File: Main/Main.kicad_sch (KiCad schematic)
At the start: 95 parts, among them J1 USB_B_Micro, J2 XT60, J3 Conn_01x03, J4 Conn_01x03, J5 Conn_01x03, J6 Conn_01x03, J7 MSD-4-A, Q2 Si2301CDS, SW1 SW_Push, SW2 SW_Push, U1 RP2350A-QFN60, U10 LM75B, U11 MCS1802GS-50-Z, U12 MCS1802GS-50-Z, U13 MCS1802GS-50-Z, U15 AP62150WU, U2 W25Q128JVS, U3 AMS1117-3.3, U4 MMC5983MA, U5 ICM-42688-P, U6 INA226, U7 KX134-1211, U8 MS5611-01BA, U9 MCS1802GS-50-Z, Y1 ABM8-272-T3

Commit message: more layout updates and small fixes
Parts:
- D1: value LED -> RED_LED
- D2: value LED -> BLUE_LED
- D3: value LED -> GREEN_LED
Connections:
- net ACCEL_SDI/SDA is gone; now on net SPI_SDI: U7.2 (SDI/SDA)
- net ACCEL_SDO/ADDR is gone; now on net SPI_SD0: U7.1 (SDO/ADDR)
- net GND: now also C29.2, C30.2; no longer R13.1, U6.8 (Vbus), U6.9 (Vin-)
- net VIN: now also R13.1, U6.9 (Vin-); no longer J2.2 (Pin_2)
- net VSS: no longer names the net of R13.2, U6.10 (Vin+)
- net VSS: now also J2.2 (Pin_2), U6.8 (Vbus)
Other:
- moved on the sheet: C24, C39, C40, C41, D1, D2, D3, J2, L3, Q2, R10, R11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

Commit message: more layout updates
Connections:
- net SCL: now also U1.33 (GPIO21)
- net SDA: now also U1.32 (GPIO20)
- net Vout1: now also U1.40 (GPIO26_ADC0)
- net Vout2: now also U1.41 (GPIO27_ADC1)
- net Vout3: now also U1.43 (GPIO29_ADC3)
- net Vout4: now also U1.42 (GPIO28_ADC2)
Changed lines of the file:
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@@
+		)
+	)
+	(global_label "Vout1"
+		(shape input)
+		(at 212.09 143.51 0)
+		(fields_autoplaced yes)
+		(effects
+			(font
+				(size 1.27 1.27)
+			)
+			(justify left)
+		)
+		(property "Intersheetrefs" "${INTERSHEET_REFS}"
+			(at 220.397 143.51 0)
+			(effects
+				(font
+					(size 1.27 1.27)
+				)
+				(justify left)
+				(hide yes)
+			)
 		)
 	)
@@
 		)
 	)
+	(global_label "Vout4"
+		(shape input)
+		(at 212.09 148.59 0)
+		(fields_autoplaced yes)
+		(effects
+			(font
+				(size 1.27 1.27)
+			)
+			(justify left)
+		)
+		(property "Intersheetrefs" "${INTERSHEET_REFS}"
+			(at 220.397 148.59 0)
+			(effects
+				(font
+					(size 1.27 1.27)
+				)
+				(justify left)
+				(hide yes)
+			)
+		)
+	)
 	(global_label "SPI_SDI"
 		(shape input)
@@
 		)
 	)
+	(global_label "SDA"
+		(shape input)
+		(at 212.09 125.73 0)
+		(fields_autoplaced yes)
+		(effects
+			(font
+				(size 1.27 1.27)
+			)
+			(justify left)
+		)
+		(property "Intersheetrefs" "${INTERSHEET_REFS}"
+			(at 218.6433 125.73 0)
+			(effects
+				(font
+					(size 1.27 1.27)
+				)
+				(justify left)
+				(hide yes)
+			)
+		)
+	)
 	(global_label "current -1"
 		(shape input)
@@
 		)
 	)
+	(global_label "Vout3"
+		(shape input)
+		(at 212.09 151.13 0)
+		(fields_autoplaced yes)
+		(effects
+			(font
+				(size 1.27 1.27)
+			)
+			(justify left)
+		)
+		(property "Intersheetrefs" "${INTERSHEET_REFS}"
+			(at 220.397 151.13 0)
+			(effects
+				(font
+					(size 1.27 1.27)
+				)
+				(justify left)
+				(hide yes)
+			)
+		)
+	)
 	(global_label "SPI_SDI2"
 		(shape input)
@@
 				)
 				(justify right)
+				(hide yes)
+			)
+		)
+	)
+	(global_label "Vout2"
+		(shape input)
+		(at 212.09 146.05 0)
+		(fields_autoplaced yes)
+		(effects
+			(font
+				(size 1.27 1.27)
+			)
+			(justify left)
+		)
+		(property "Intersheetrefs" "${INTERSHEET_REFS}"
+			(at 220.397 146.05 0)
+			(effects
+				(font
+					(size 1.27 1.27)
+				)
+				(justify left)
 				(hide yes)
 			)
@@
 			(effects
 				(font
+					(size 1.27 1.27)
+				)
+				(justify left)
+				(hide yes)
+			)
+		)
+	)
+	(global_label "SCL"
+		(shape input)
+		(at 212.09 128.27 0)
+		(fields_autoplaced yes)
+		(effects
+			(font
+				(size 1.27 1.27)
+			)
+			(justify left)
+		)
+		(property "Intersheetrefs" "${INTERSHEET_REFS}"
+			(at 218.5828 128.27 0)
+			(effects
+				(font

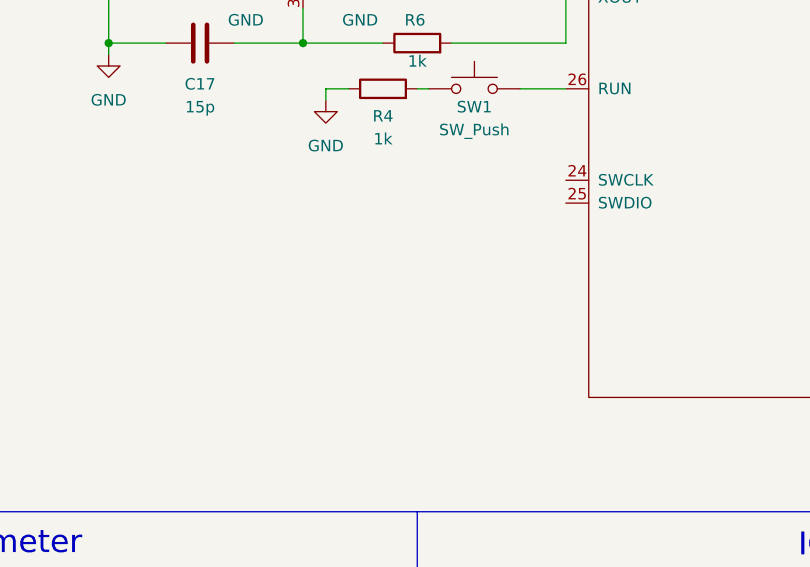
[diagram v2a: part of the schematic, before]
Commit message: updated layout
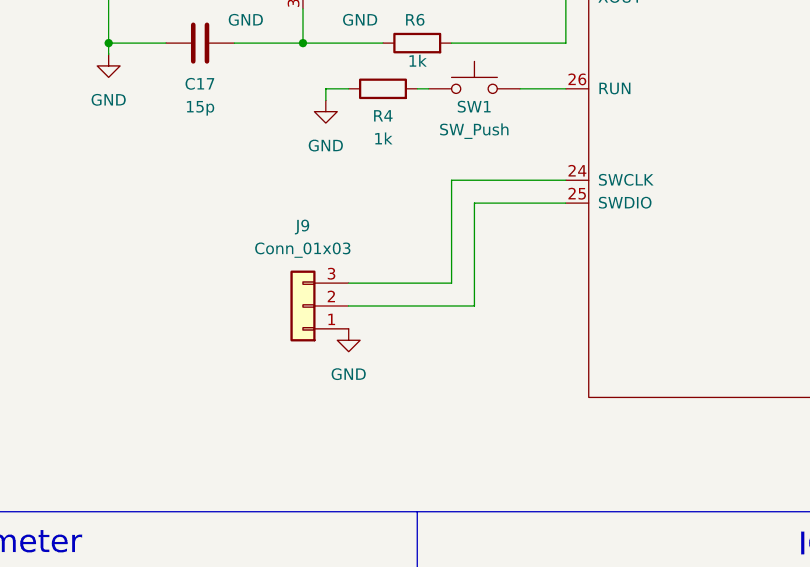
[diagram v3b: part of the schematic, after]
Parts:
- added J9: Conn_01x03, Connector_PinHeader_2.54mm:PinHeader_1x03_P2.54mm_Vertical, symbol Connector_Generic:Conn_01x03
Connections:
- net GND: now also J9.1 (Pin_1)
- net at U1.24 (SWCLK): now also J9.3 (Pin_3)
- net at U1.25 (SWDIO): now also J9.2 (Pin_2)
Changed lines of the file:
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@@
 	(wire
 		(pts
+			(xy 149.86 133.35) (xy 139.7 133.35)
+		)
+		(stroke
+			(width 0)
+			(type default)
+		)
+	)
+	(wire
+		(pts
 			(xy 137.16 60.96) (xy 137.16 62.23)
 		)
@@
 	(wire
 		(pts
+			(xy 125.73 144.78) (xy 139.7 144.78)
+		)
+		(stroke
+			(width 0)
+			(type default)
+		)
+	)
+	(wire
+		(pts
 			(xy 114.3 107.95) (xy 115.57 107.95)
 		)
@@
 	(wire
 		(pts
+			(xy 137.16 130.81) (xy 137.16 142.24)
+		)
+		(stroke
+			(width 0)
+			(type default)
+		)
+	)
+	(wire
+		(pts
 			(xy 345.44 194.31) (xy 347.98 194.31)
 		)
@@
 		)
 	)
+	(wire
+		(pts
+			(xy 137.16 142.24) (xy 125.73 142.24)
+		)
+		(stroke
+			(width 0)
+			(type default)
+		)
+	)
 	(polyline
 		(pts
@@
 	(wire
 		(pts
+			(xy 139.7 133.35) (xy 139.7 144.78)
+		)
+		(stroke
+			(width 0)
+			(type default)
+		)
+	)
+	(wire
+		(pts
 			(xy 22.86 193.04) (xy 34.29 193.04)
 		)
@@
 	(wire
 		(pts
+			(xy 149.86 130.81) (xy 137.16 130.81)
+		)
+		(stroke
+			(width 0)
+			(type default)
+		)
+	)
+	(wire
+		(pts
 			(xy 24.13 44.45) (xy 26.67 44.45)
 		)
@@
 	)
 	(symbol
+		(lib_id "Connector_Generic:Conn_01x03")
+		(at 120.65 144.78 180)
+		(unit 1)
+		(exclude_from_sim no)
+		(in_bom yes)
+		(on_board yes)
+		(dnp no)
+		(fields_autoplaced yes)
+		(property "Reference" "J9"
+			(at 120.65 135.89 0)
+			(effects
+				(font
+					(size 1.27 1.27)
+				)
+			)
+		)
+		(property "Value" "Conn_01x03"
+			(at 120.65 138.43 0)
+			(effects
+				(font
+					(size 1.27 1.27)
+				)
+			)
+		)
+		(property "Footprint" "Connector_PinHeader_2.54mm:PinHeader_1x03_P2.54mm_Vertical"
+			(at 120.65 144.78 0)
+			(effects
+				(font
+					(size 1.27 1.27)
+				)
+				(hide yes)
+			)
+		)
+		(property "Datasheet" "~"
+			(at 120.65 144.78 0)
+			(effects
+				(font
+					(size 1.27 1.27)
+				)
+				(hide yes)
+			)
+		)
+		(property "Description" "Generic connector, single row, 01x03, script generated (kicad-library-utils/schlib/autogen/connector/)"
+			(at 120.65 144.78 0)
+			(effects
+				(font
+					(size 1.27 1.27)
+				)
+				(hide yes)
+			)
+		)
+		(property "JLCPCB Part #" ""
+			(at 120.65 144.78 0)
+			(effects
+				(font
+					(size 1.27 1.27)
+				)
+				(hide yes)
+			)
+		)
+		(property "Sim.Device" ""
+			(at 120.65 144.78 0)
+			(effects
+				(font
+					(size 1.27 1.27)
+				)
+				(hide yes)
+			)
+		)
+		(pin "1"
+		)
+		(pin "2"
+		)
+		(pin "3"
+		)
+		(instances
+			(project "Main"
+				(path "/6b66026e-3aa1-4d5a-a331-be21386153c7"
+					(reference "J9")
+					(unit 1)
+				)
+			)
+		)
+	)
+	(symbol
 		(lib_id "power:GND")
 		(at 502.92 86.36 0)
@@
 					(unit 1)
 				)
+			)
+		)
+	)
+	(symbol
+		(lib_id "power:GND")
+		(at 125.73 147.32 0)
+		(unit 1)
+		(exclude_from_sim no)
+		(in_bom yes)
+		(on_board yes)
+		(dnp no)
+		(fields_autoplaced yes)
+		(property "Reference" "#PWR030"
+			(at 125.73 153.67 0)
+			(effects
+				(font
+					(size 1.27 1.27)
+				)
+				(hide yes)
+			)
+		)
+		(property "Value" "GND"
+			(at 125.73 152.4 0)
+			(effects
+				(font
+					(size 1.27 1.27)
+				)
+			)
+		)
+		(property "Footprint" ""
+			(at 125.73 147.32 0)
+			(effects
+				(font
+					(size 1.27 1.27)
+				)
+				(hide yes)
+			)
+		)
+		(property "Datasheet" ""
+			(at 125.73 147.32 0)
+			(effects
+				(font
+					(size 1.27 1.27)
+				)
+				(hide yes)
+			)
+		)
+		(property "Description" "Power symbol creates a global label with name \"GND\" , ground"
+			(at 125.73 147.32 0)
+			(effects
+				(font
+					(size 1.27 1.27)
+				)
+				(hide yes)
+			)
+		)
+		(pin "1"
+		)
+		(instances
+			(project "Main"
+				(path "/6b66026e-3aa1-4d5a-a331-be21386153c7"
+					(reference "#PWR030")
+					(unit 1)
+				)

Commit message: updated power switching schematic
still need to fix footprint tsp
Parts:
- removed Q2: Si2301CDS, Package_TO_SOT_SMD:SOT-23, symbol Transistor_FET:Si2319CDS
- removed R22: 100k, Resistor_SMD:R_0402_1005Metric, symbol Device:R
- added C35: 1u, Capacitor_SMD:C_0805_2012Metric, symbol Device:C_Small
- added R19, R27: 30k, Resistor_SMD:R_0603_1608Metric, symbol Device:R_Small_US
- added R24, R25, R26: 100k, Resistor_SMD:R_0603_1608Metric, symbol Device:R_Small_US
- added U14: TPS2121RUXR, TPS2121:IC_TPS2121RUXR, symbol TPS2121RUXR:TPS2121RUXR
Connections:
- net +3.3V: no longer C21.1, U3.2 (VO)
- net GND: now also C35.2, R24.2, R26.2, R27.2, U14.12 (GND), U14.4 (OV2), U14.5 (OV1), U14.9 (ST)
- net 3.3v_Batt: now reaches C41.1, L3.1, R20.1
- net 3.3v_Batt: now also R25.1, U14.2 (IN2), U14.2_1 (IN2)
- new net: R25.2, R26.1, U14.3 (CP2)
- new net: R19.2, R24.1, U14.6 (PR1)
- new net: R27.1, U14.10 (ILIM)
- new net: C35.1, U14.11 (SS)
- new net 3.3v_usb: C21.1, R19.1, U14.7 (IN1), U14.7_1 (IN1), U3.2 (VO)
- new net OUT: U14.1 (OUT), U14.1_1 (OUT), U14.8 (OUT), U14.8_1 (OUT)
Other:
- note removed: "Blocks Connection when USB plugged in to prevent backpowering"

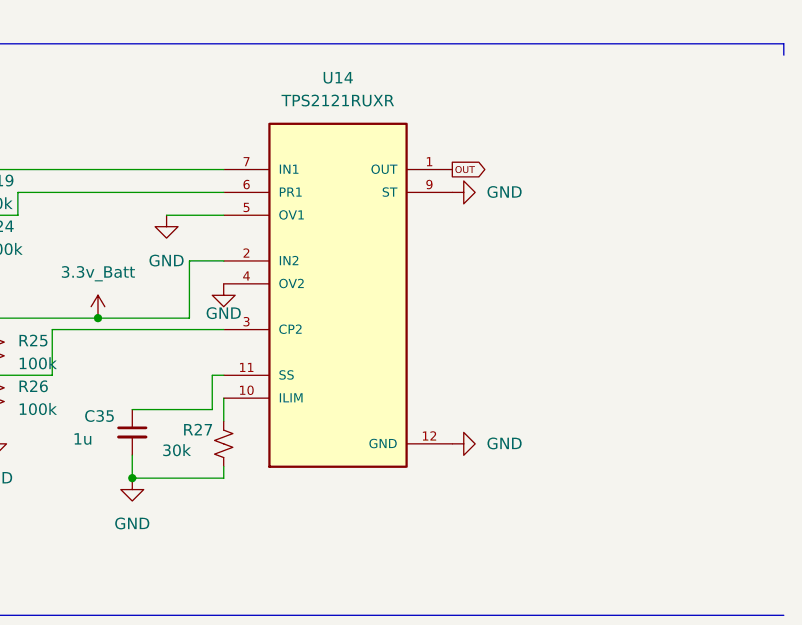
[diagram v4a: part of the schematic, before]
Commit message: updated power switching circuit
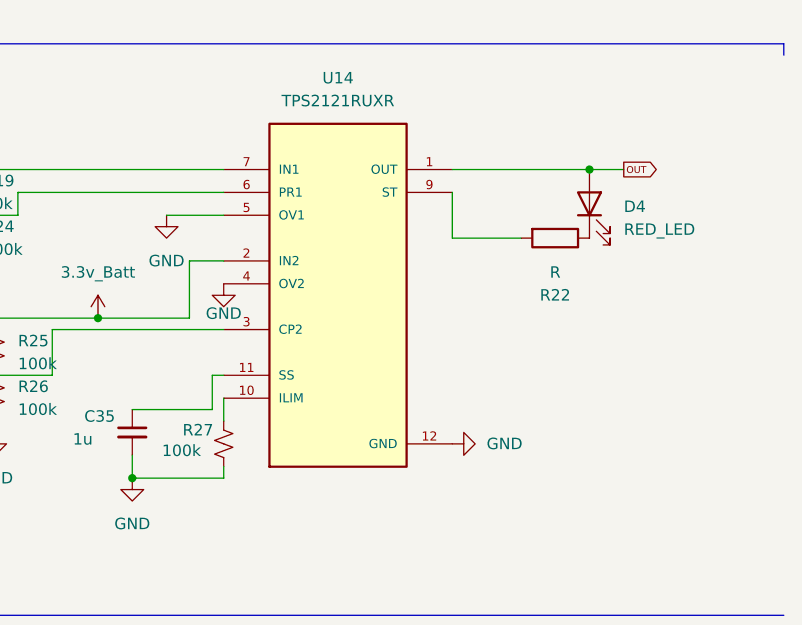
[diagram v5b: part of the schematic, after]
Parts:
- added D4: RED_LED, LED_SMD:LED_0805_2012Metric, symbol Device:LED
- added R22: R, Resistor_SMD:R_0402_1005Metric, symbol Device:R
- R19, R20, R24, R25, R26: footprint Resistor_SMD:R_0603_1608Metric -> Resistor_SMD:R_0402_1005Metric
- R27: value 30k -> 100k; footprint Resistor_SMD:R_0603_1608Metric -> Resistor_SMD:R_0402_1005Metric
- U14: footprint TPS2121:IC_TPS2121RUXR -> Package_DFN_QFN:Texas_VQFN-HR-12_2x2.5mm_P0.5mm_ThermalVias
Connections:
- net GND: no longer U14.9 (ST)
- net OUT: now also D4.2 (A)
- new net: D4.1 (K), R22.1
- new net: R22.2, U14.9 (ST)
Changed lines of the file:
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@@
 	)
 	(junction
+		(at 560.07 181.61)
+		(diameter 0)
+		(color 0 0 0 0)
+	)
+	(junction
 		(at 234.95 187.96)
 		(diameter 0)
@@
 	(wire
 		(pts
+			(xy 563.88 181.61) (xy 560.07 181.61)
+		)
+		(stroke
+			(width 0)
+			(type default)
+		)
+	)
+	(wire
+		(pts
 			(xy 116.84 175.26) (xy 116.84 198.12)
 		)
@@
 	(wire
 		(pts
+			(xy 544.83 189.23) (xy 544.83 184.15)
+		)
+		(stroke
+			(width 0)
+			(type default)
+		)
+	)
+	(wire
+		(pts
 			(xy 481.33 139.7) (xy 463.55 139.7)
 		)
@@
 	(wire
 		(pts
+			(xy 560.07 181.61) (xy 544.83 181.61)
+		)
+		(stroke
+			(width 0)
+			(type default)
+		)
+	)
+	(wire
+		(pts
 			(xy 515.62 191.77) (xy 519.43 191.77)
 		)
@@
 	(wire
 		(pts
+			(xy 552.45 189.23) (xy 544.83 189.23)
+		)
+		(stroke
+			(width 0)
+			(type default)
+		)
+	)
+	(wire
+		(pts
 			(xy 156.21 276.86) (xy 166.37 276.86)
 		)
@@
 	(global_label "OUT"
 		(shape output)
-		(at 544.83 181.61 0)
+		(at 563.88 181.61 0)
 		(fields_autoplaced yes)
 		(effects
@@
 		)
 		(property "Intersheetrefs" "${INTERSHEET_REFS}"
-			(at 548.7986 181.61 0)
+			(at 567.8486 181.61 0)
 			(effects
 				(font
@@
 			)
 		)
-		(property "Footprint" "Resistor_SMD:R_0603_1608Metric"
+		(property "Footprint" "Resistor_SMD:R_0402_1005Metric"
 			(at 494.03 201.93 0)
 			(effects
@@
 			)
 		)
-		(property "Footprint" "Resistor_SMD:R_0603_1608Metric"
+		(property "Footprint" "Resistor_SMD:R_0402_1005Metric"
 			(at 490.22 189.23 0)
 			(effects
@@
 	)
 	(symbol
+		(lib_id "Device:LED")
+		(at 560.07 185.42 90)
+		(unit 1)
+		(exclude_from_sim no)
+		(in_bom yes)
+		(on_board yes)
+		(dnp no)
+		(fields_autoplaced yes)
+		(property "Reference" "D4"
+			(at 563.88 185.7374 90)
+			(effects
+				(font
+					(size 1.27 1.27)
+				)
+				(justify right)
+			)
+		)
+		(property "Value" "RED_LED"
+			(at 563.88 188.2774 90)
+			(effects
+				(font
+					(size 1.27 1.27)
+				)
+				(justify right)
+			)
+		)
+		(property "Footprint" "LED_SMD:LED_0805_2012Metric"
+			(at 560.07 185.42 0)
+			(effects
+				(font
+					(size 1.27 1.27)
+				)
+				(hide yes)
+			)
+		)
+		(property "Datasheet" "~"
+			(at 560.07 185.42 0)
+			(effects
+				(font
+					(size 1.27 1.27)
+				)
+				(hide yes)
+			)
+		)
+		(property "Description" "Light emitting diode"
+			(at 560.07 185.42 0)
+			(effects
+				(font
+					(size 1.27 1.27)
+				)
+				(hide yes)
+			)
+		)
+		(property "Sim.Pins" "1=K 2=A"
+			(at 560.07 185.42 0)
+			(effects
+				(font
+					(size 1.27 1.27)
+				)
+				(hide yes)
+			)
+		)
+		(property "JLCPCB Part #" ""
+			(at 560.07 185.42 0)
+			(effects
+				(font
+					(size 1.27 1.27)
+				)
+				(hide yes)
+			)
+		)
+		(property "Sim.Device" ""
+			(at 560.07 185.42 0)
+			(effects
+				(font
+					(size 1.27 1.27)
+				)
+				(hide yes)
+			)
+		)
+		(pin "2"
+		)
+		(pin "1"
+		)
+		(instances
+			(project "Main"
+				(path "/6b66026e-3aa1-4d5a-a331-be21386153c7"
+					(reference "D4")
+					(unit 1)
+				)
+			)
+		)
+	)
+	(symbol
 		(lib_id "power:GND")
 		(at 502.92 86.36 0)
@@
 			)
 		)
-		(property "Value" "30k"
+		(property "Value" "100k"
 			(at 512.572 212.852 0)
 			(effects
@@
 			)
 		)
-		(property "Footprint" "Resistor_SMD:R_0603_1608Metric"
+		(property "Footprint" "Resistor_SMD:R_0402_1005Metric"
 			(at 519.43 212.09 0)
 			(effects
@@
 			)
 		)
-		(property "Footprint" "Resistor_SMD:R_0603_1608Metric"
+		(property "Footprint" "Resistor_SMD:R_0402_1005Metric"
 			(at 479.552 123.19 90)
 			(effects
@@
 			)
 		)
-		(property "Footprint" "TPS2121:IC_TPS2121RUXR"
+		(property "Footprint" "Package_DFN_QFN:Texas_VQFN-HR-12_2x2.5mm_P0.5mm_ThermalVias"
 			(at 532.13 196.85 0)
 			(effects
@@
 	(symbol
 		(lib_id "power:GND")
-		(at 544.83 184.15 90)
-		(unit 1)
-		(exclude_from_sim no)
-		(in_bom yes)
-		(on_board yes)
-		(dnp no)
-		(fields_autoplaced yes)
-		(property "Reference" "#PWR083"
-			(at 551.18 184.15 0)
-			(effects
-				(font
-					(size 1.27 1.27)
-				)
-				(hide yes)
-			)
-		)
-		(property "Value" "GND"
-			(at 548.64 184.1499 90)
-			(effects
-				(font
-					(size 1.27 1.27)
-				)
-				(justify right)
-			)
-		)
-		(property "Footprint" ""
-			(at 544.83 184.15 0)
-			(effects
-				(font
-					(size 1.27 1.27)
-				)
-				(hide yes)
-			)
-		)
-		(property "Datasheet" ""
-			(at 544.83 184.15 0)
-			(effects
-				(font
-					(size 1.27 1.27)
-				)
-				(hide yes)
-			)
-		)
-		(property "Description" "Power symbol creates a global label with name \"GND\" , ground"
-			(at 544.83 184.15 0)
-			(effects
-				(font
-					(size 1.27 1.27)
-				)
-				(hide yes)
-			)
-		)
-		(pin "1"
-		)
-		(instances
-			(project "Main"
-				(path "/6b66026e-3aa1-4d5a-a331-be21386153c7"
-					(reference "#PWR083")
-					(unit 1)
-				)
-			)
-		)
-	)
-	(symbol
-		(lib_id "power:GND")
 		(at 303.53 266.7 0)
 		(unit 1)
@@
 	)
 	(symbol
+		(lib_id "Device:R")
+		(at 556.26 189.23 270)
+		(unit 1)
+		(exclude_from_sim no)
+		(in_bom yes)
+		(on_board yes)
+		(dnp no)
+		(fields_autoplaced yes)
+		(property "Reference" "R22"
+			(at 556.26 195.58 90)
+			(effects
+				(font
+					(size 1.27 1.27)
+				)
+			)
+		)
+		(property "Value" "R"
+			(at 556.26 193.04 90)
+			(effects
+				(font
+					(size 1.27 1.27)
+				)
+			)
+		)
+		(property "Footprint" "Resistor_SMD:R_0402_1005Metric"
+			(at 556.26 187.452 90)
+			(effects
+				(font
+					(size 1.27 1.27)
+				)
+				(hide yes)
+			)
+		)
+		(property "Datasheet" "~"
+			(at 556.26 189.23 0)
+			(effects
+				(font
+					(size 1.27 1.27)
+				)
+				(hide yes)
+			)
+		)
+		(property "Description" "Resistor"
+			(at 556.26 189.23 0)
+			(effects
+				(font
+					(size 1.27 1.27)
+				)
+				(hide yes)
+			)
+		)
+		(property "JLCPCB Part #" ""
+			(at 556.26 189.23 90)
+			(effects
+				(font
+					(size 1.27 1.27)
+				)
+				(hide yes)
+			)
+		)
+		(property "Sim.Device" ""
+			(at 556.26 189.23 90)
+			(effects
+				(font
+					(size 1.27 1.27)
+				)
+				(hide yes)
+			)
+		)
+		(pin "1"
+		)
+		(pin "2"
+		)
+		(instances
+			(project "Main"
+				(path "/6b66026e-3aa1-4d5a-a331-be21386153c7"
+					(reference "R22")
+					(unit 1)
+				)
+			)
+		)
+	)
+	(symbol
 		(lib_id "power:+1V1")
 		(at 116.84 67.31 0)
@@
 			)
 		)
-		(property "Footprint" "Resistor_SMD:R_0603_1608Metric"
+		(property "Footprint" "Resistor_SMD:R_0402_1005Metric"
 			(at 494.03 207.01 0)
 			(effects
@@
 			)
 		)
-		(property "Footprint" "Resistor_SMD:R_0603_1608Metric"
+		(property "Footprint" "Resistor_SMD:R_0402_1005Metric"
 			(at 490.22 184.15 0)
 			(effects
